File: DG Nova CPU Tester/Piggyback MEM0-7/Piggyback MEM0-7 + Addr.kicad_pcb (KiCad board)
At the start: 2 copper layers, 73.9 x 53.5 mm, 28 parts, among them J1 Conn_02x18_Odd_Even, J2 Arduino Digital Pins, J22 Arduino Digital Pins, J23 Arduino Digital Pins, J3 Conn_01x17, J4 Arduino Digital Pins, SW1 Arduino Mega Reset, U1 74LS03, U2 74LS03, U3 74LS04, U4 74HC595, U5 74LS03, U6 74LS03, U7 74LS03, U8 74LS03, U9 74HC595

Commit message: more
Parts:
- removed J22: Arduino Digital Pins, Connector_PinHeader_2.54mm:PinHeader_1x05_P2.54mm_Vertical
- removed J23: Arduino Digital Pins, Connector_PinHeader_2.54mm:PinHeader_1x06_P2.54mm_Vertical
- C1, C2, C3, C4, C5, C6, C7, C8, C9: footprint Forgotten Machines:Disc Capacitor Common Entrex Trapezoid -> Forgotten Machines:Disc Capacitor Entrex Trapezoid .10
- moved C6 129.9 mm to (75.4, 112.0), turned to 90 degrees
- moved C7 123.2 mm to (75.4, 102.1), turned to 90 degrees
- moved C1 113.2 mm to (77.0, 90.0)
- moved C9 99.7 mm to (92.5, 90.0)
- moved C8 91.5 mm to (102.9, 90.0)
- moved C3 80.2 mm to (109.0, 90.0)
- moved C4 73.5 mm to (114.8, 90.0)
- moved C2 61.9 mm to (124.5, 68.3)
- moved C5 56.1 mm to (130.7, 68.3)
- moved U3 1.52 mm to (108.5, 93.2)
- moved U4 0.38 mm to (78.6, 106.0)
- moved U9 0.38 mm to (78.6, 116.1)
- renumbered DIP4 to SW2
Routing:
- net CON DATA: track 0.00 -> 148.6 mm
- net CON INST: track 0.00 -> 80.9 mm
- net ~{MEM8}: track 0.00 -> 74.9 mm
- net ~{MEM11}: track 0.00 -> 71.7 mm, vias 0 -> 3
- net ~{MEM3}: track 0.00 -> 70.3 mm
- net ~{MEM10}: track 0.00 -> 68.8 mm
- net ~{MEM0}: track 0.00 -> 61.8 mm
- net ~{MEM9}: track 0.00 -> 59.6 mm
- net ~{MEM14}: track 0.00 -> 59.1 mm
- net ~{MEM12}: track 0.00 -> 55.0 mm
- net ~{MEM15}: track 0.00 -> 54.4 mm
- net ~{MEM1}: track 0.00 -> 48.4 mm
- net ~{MEM13}: track 0.00 -> 46.9 mm
- net Addr11: track 0.00 -> 45.9 mm
- net ~{MEM4}: track 0.00 -> 38.3 mm
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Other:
- copper layers 2 -> 4

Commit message: build
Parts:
- removed ?: , 
- moved U7 11.7 mm to (130.0, 71.6)
- moved U8 10.3 mm to (118.9, 71.6)
- moved C5 3.18 mm to (133.5, 66.8)
- moved C2 1.52 mm to (124.5, 66.8)
- moved C7 0.13 mm to (75.4, 102.2), turned to -90 degrees
- turned C3 to 180 degrees
- turned C4 to 180 degrees
- turned C6 to -90 degrees
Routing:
- net Addr12: track 0.00 -> 104.1 mm
- net Addr15: track 0.00 -> 89.4 mm, vias 0 -> 1
- net Addr03: track 0.00 -> 88.3 mm
- net Addr14: track 0.00 -> 80.5 mm, vias 0 -> 2
- net Addr09: track 0.00 -> 78.1 mm, vias 0 -> 2
- net Addr13: track 0.00 -> 74.6 mm, vias 0 -> 2
- net Addr00: track 0.00 -> 69.5 mm
- net ClockPin2: track 0.00 -> 63.2 mm
- net Addr08: track 18.0 -> 80.5 mm
- net Addr07: track 0.00 -> 55.9 mm, vias 0 -> 2
- net Addr01: track 0.00 -> 55.7 mm
- net Addr02: track 0.00 -> 54.6 mm
- net ~{MEM2}: track 0.00 -> 53.5 mm
- net LatchPin2: track 0.00 -> 51.9 mm, vias 0 -> 2
- net Addr06: track 0.00 -> 50.6 mm, vias 0 -> 2
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- added copper zone on B.Cu, net +5V
- added copper zone on In1.Cu, net GND

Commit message: Done?
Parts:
- removed XA1: Arduino_Mega2560_Shield, Forgotten Machines:Arduino_Mega2560_Shield
- added J5: Conn_01x08, Connector_PinHeader_2.54mm:PinHeader_1x08_P2.54mm_Vertical, F.Cu at (79.6, 116.0)
- added J6: Conn_01x08, Connector_PinHeader_2.54mm:PinHeader_1x08_P2.54mm_Vertical, F.Cu at (102.5, 116.0)
- moved C6 62.8 mm to (137.0, 99.9), turned to 0 degrees
- moved U9 45.9 mm to (120.5, 97.3)
- moved SW2 1.40 mm to (120.5, 108.6)
- renumbered SW1 to Button
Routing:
- net Addr12: track 104.1 -> 40.7 mm
- net Addr15: track 89.4 -> 26.2 mm, vias 1 -> 0
- net Addr08: track 80.5 -> 17.2 mm
- net Addr09: track 78.1 -> 17.1 mm, vias 2 -> 0
- net Addr14: track 80.5 -> 19.7 mm, vias 2 -> 1
- net Addr10: track 78.4 -> 18.1 mm, vias 0 -> 1
- net Addr11: track 83.9 -> 25.0 mm, vias 2 -> 0
- net Addr13: track 74.6 -> 17.0 mm, vias 2 -> 0
- net ClockPin2: track 63.2 -> 25.4 mm
- net LatchPin2: track 51.9 -> 25.6 mm, vias 2 -> 1
- net ~{CON DATA}: track 0.00 -> 20.1 mm
- net DataPin2: track 37.9 -> 29.6 mm
- net LatchPin1: track 34.2 -> 36.6 mm
- net DataPin1: track 32.7 -> 35.1 mm
- net ClockPin1: track 27.6 -> 30.0 mm
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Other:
- board text added: "Arduino Mega Reset"
- board text added: "DIP4"
- board text added: "~{CON DATA}"
- board text added: "~{CONT+ISTP+MSTP}"
- board text added: "~{MBO1}"
- board text added: "~{MBO2}"
- board text added: "~{MBO3}"
- board text added: "~{MBO4}"
- board text added: "~{MBO5}"
- board text added: "~{MBO6}"
- board text added: "~{MBO7}"
- board text added: "~{STOP}"

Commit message: gerbers
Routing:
- net Addr06: track 50.9 -> 46.2 mm
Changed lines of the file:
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@@
       (outputformat 1)
       (mirror false)
-      (drillshape 1)
+      (drillshape 0)
       (scaleselection 1)
       (outputdirectory "")
@@
       (xy 131.873416 109.93013)
       (xy 131.87236 110.421667)
-      (xy 131.87236 110.421667)
       (xy 131.87203 110.424268)
       (xy 131.871714 110.427204)
@@
       (xy 131.871284 108.772783)
       (xy 131.871286 108.772783)
-      (xy 131.871286 108.772783)
       (xy 131.871287 108.772783)
       (xy 131.871288 108.772783)
@@
   (segment (start 99.296 106.299) (end 97.917 104.92) (width 0.25) (layer "In2.Cu") (net 72))
   (segment (start 101.727 93.091) (end 102.362 93.091) (width 0.25) (layer "In2.Cu") (net 72))
-  (segment (start 104.267 81.788) (end 100.925 85.13) (width 0.25) (layer "In2.Cu") (net 72))
   (segment (start 104.267 81.788) (end 100.475 85.58) (width 0.25) (layer "In2.Cu") (net 72))
   (segment (start 106.553 106.299) (end 106.839 106.013) (width 0.25) (layer "F.Cu") (net 73))

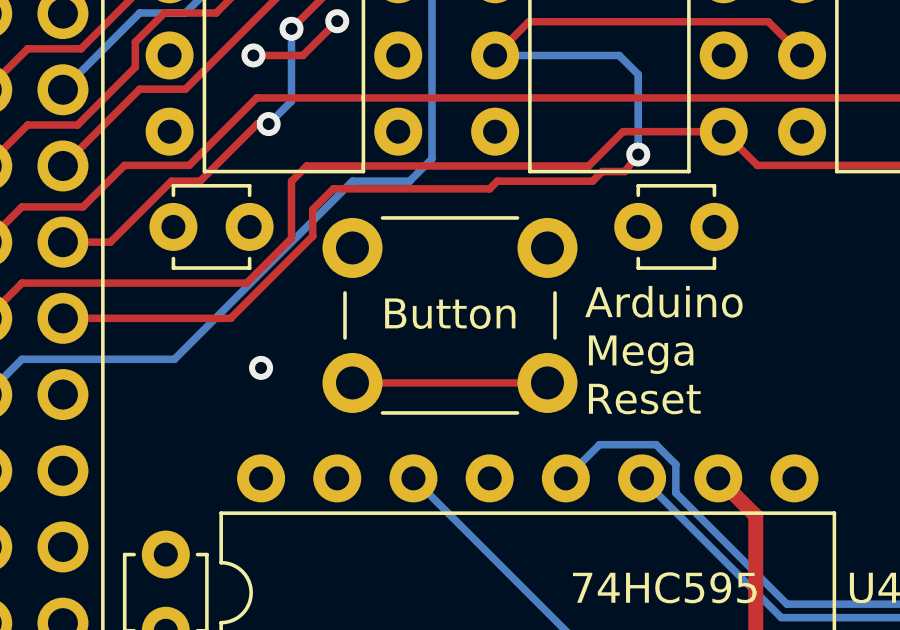
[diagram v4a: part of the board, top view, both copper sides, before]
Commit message: fix /CE to GND
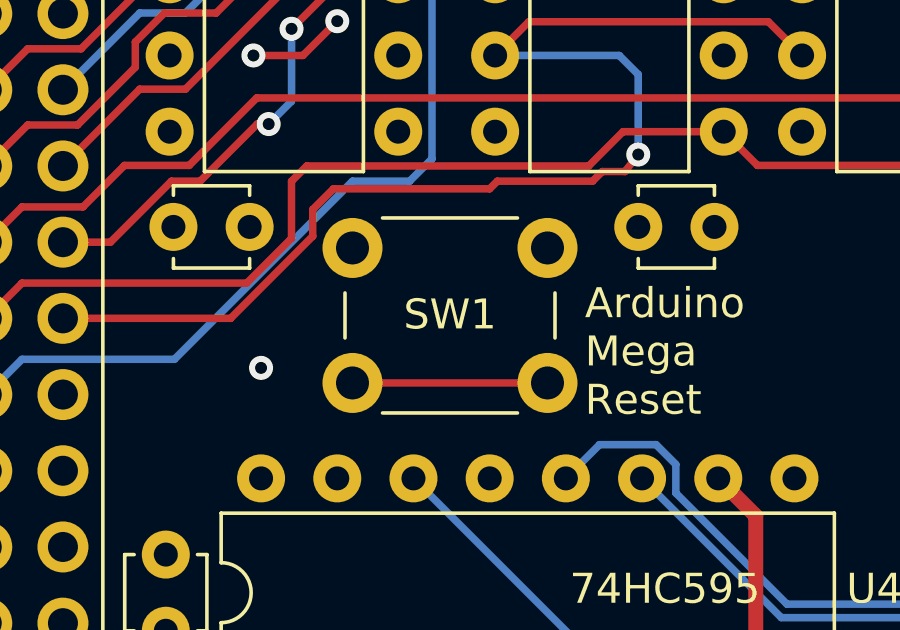
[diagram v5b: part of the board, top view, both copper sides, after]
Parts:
- renumbered Button to SW1
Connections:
- U4 pad 13: unconnected-(U4-~{OE}-Pad13) -> GND
- U9 pad 13: unconnected-(U9-~{OE}-Pad13) -> GND
